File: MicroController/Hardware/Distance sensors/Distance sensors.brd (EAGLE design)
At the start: 70 x 40 mm, 20 parts

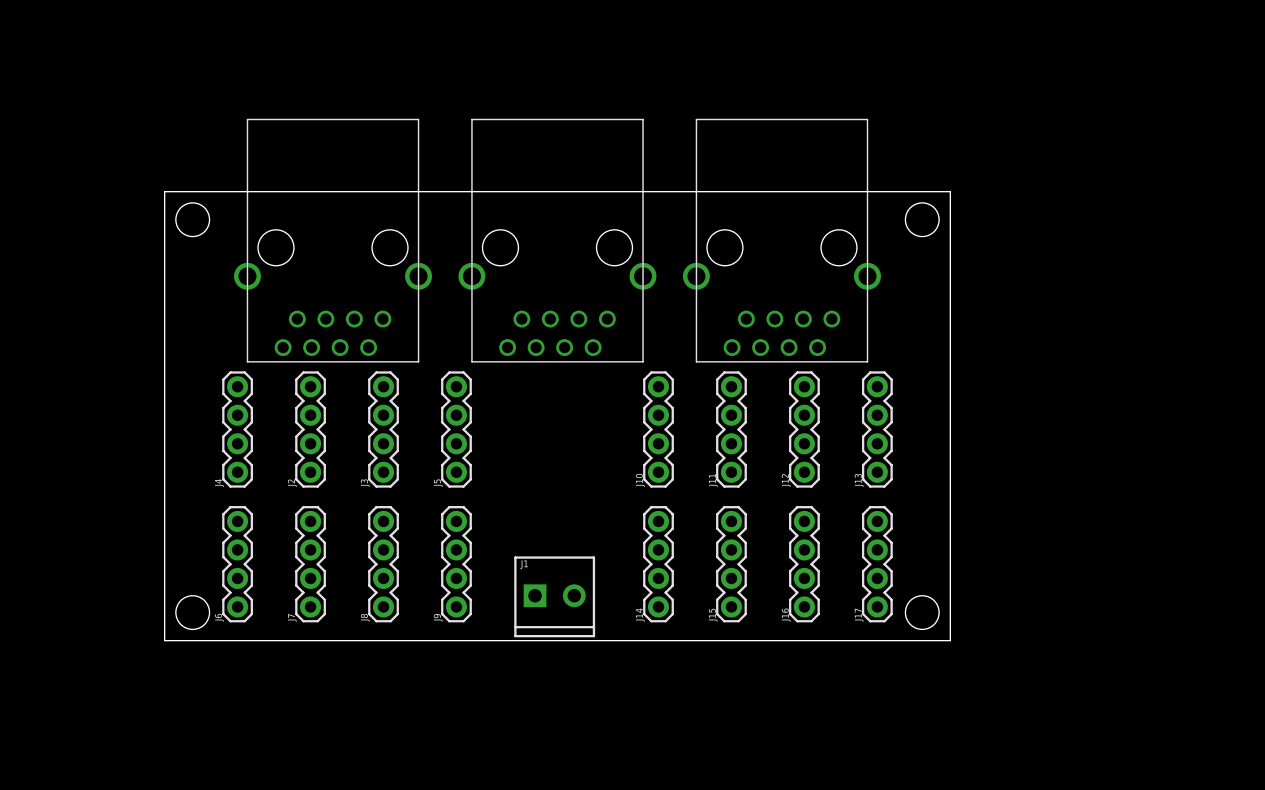
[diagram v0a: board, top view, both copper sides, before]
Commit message: Major improvements
The Ultrasone PCB is in a good place now, it has also been well implemented on the control PCB.
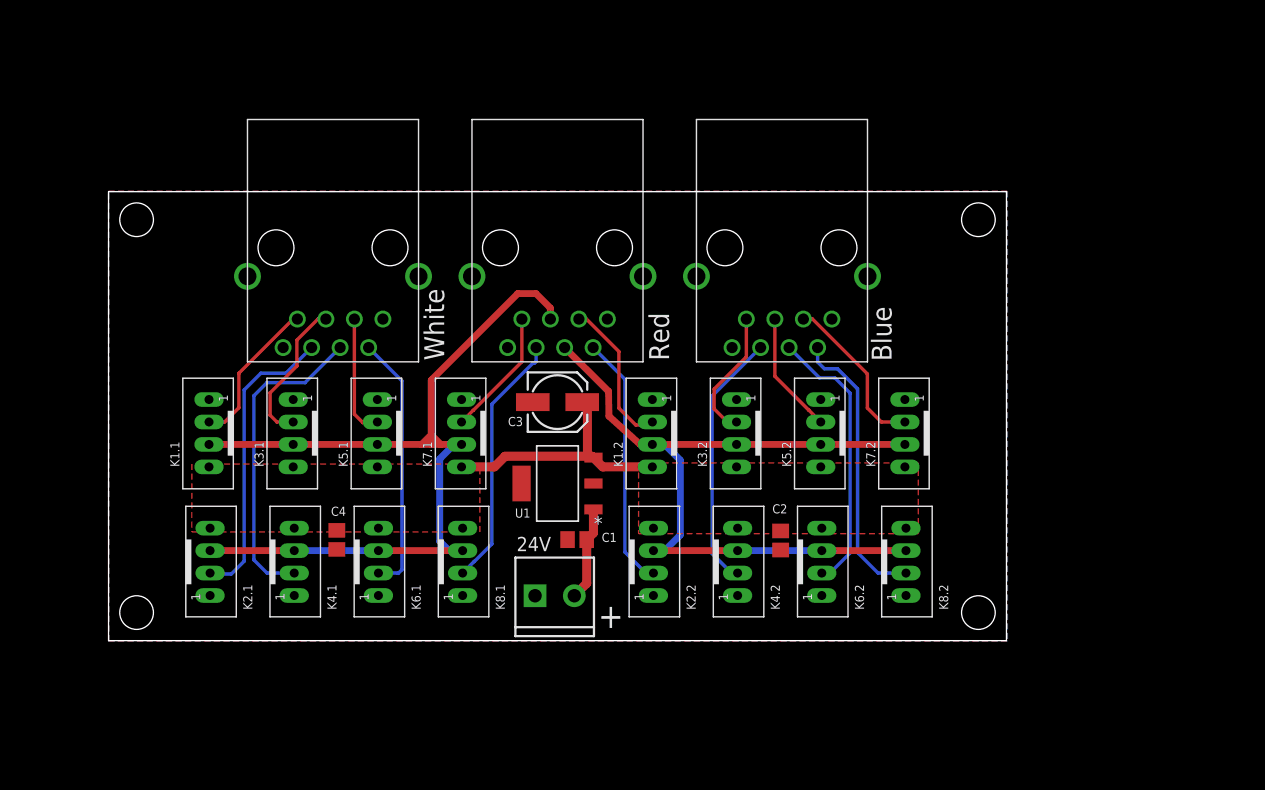
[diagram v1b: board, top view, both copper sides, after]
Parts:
- removed J10, J11, J12, J13, J14, J15, J16, J17, J2, J3, J4, J5, J6, J7, J8, J9: (no value), SparkFun-Connectors:1X04
- added C1, C2, C4: (no value), adafruit:C0805
- added C3: (no value), adafruit:153CLV-0505
- added K1.1, K1.2, K2.1, K2.2, K3.1, K3.2, K4.1, K4.2, K5.1, K5.2, K6.1, K6.2, K7.1, K7.2, K8.1, K8.2: JST-PH_4-PIN_HEADER, SRG:JST_B4B-PH_HEADER
- added U1: LM2937IMP-5.0, NSC_By_element14_Batch_1.1:SOT230P700X180-4N
- renumbered J1 to 24V
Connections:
- new net +5V: C2.1, C3.+, C4.1, K1.1.P4, K1.2.P4, K2.1.P4, K2.2.P4, K3.1.P4, K3.2.P4, K4.1.P4, K4.2.P4, K5.1.P4, K5.2.P4, K6.1.P4, K6.2.P4, K7.1.P4, K7.2.P4, K8.1.P4, K8.2.P4, U1.3
- new net GND: 24V.1, C1.2, C2.2, C3.-, C4.2, K1.1.P1, K1.2.P1, K2.1.P1, K2.2.P1, K3.1.P1, K3.2.P1, K4.1.P1, K4.2.P1, K5.1.P1, K5.2.P1, K6.1.P1, K6.2.P1, K7.1.P1, K7.2.P1, K8.1.P1, K8.2.P1, U$1.1, U$1.8, U$1.GND1, U$1.GND2, U$2.1, U$2.8, U$2.GND1, U$2.GND2, U$3.1, U$3.8, U$3.GND1, U$3.GND2, U1.2, U1.4
- new net N$1: 24V.2, C1.1, U1.1
- new net TRIGGER_1: K1.1.P3, K2.1.P3, K3.1.P3, K4.1.P3, K5.1.P3, K6.1.P3, K7.1.P3, K8.1.P3, U$2.5
- new net TRIGGER_2: K1.2.P3, K2.2.P3, K3.2.P3, K4.2.P3, K5.2.P3, K6.2.P3, K7.2.P3, K8.2.P3, U$2.4
- new net ULTRA1: K1.1.P2, U$1.7
- new net ULTRA10: K2.2.P2, U$2.2
- new net ULTRA11: K3.2.P2, U$3.7
- new net ULTRA12: K4.2.P2, U$3.6
- new net ULTRA13: K5.2.P2, U$3.5
- new net ULTRA14: K6.2.P2, U$3.4
- new net ULTRA15: K7.2.P2, U$3.3
- new net ULTRA16: K8.2.P2, U$3.2
- new net ULTRA2: K2.1.P2, U$1.6
- new net ULTRA3: K3.1.P2, U$1.5
- new net ULTRA4: K4.1.P2, U$1.4
- new net ULTRA5: K5.1.P2, U$1.3
- new net ULTRA6: K6.1.P2, U$1.2
- new net ULTRA7: K7.1.P2, U$2.7
- new net ULTRA8: K8.1.P2, U$2.6
- new net ULTRA9: K1.2.P2, U$2.3
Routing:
- net TRIGGER_1: track 0.00 -> 80.7 mm
- net TRIGGER_2: track 0.00 -> 70.3 mm
- net ULTRA4: track 0.00 -> 28.2 mm
- net ULTRA2: track 0.00 -> 26.4 mm
- net ULTRA16: track 0.00 -> 25.5 mm
- net ULTRA14: track 0.00 -> 24.6 mm
- net ULTRA6: track 0.00 -> 23.3 mm
- net ULTRA12: track 0.00 -> 23.1 mm
- net ULTRA8: track 0.00 -> 22.9 mm
- net +5V: track 0.00 -> 22.8 mm
- net ULTRA10: track 0.00 -> 22.7 mm
- net ULTRA15: track 0.00 -> 14.6 mm
- net ULTRA9: track 0.00 -> 13.5 mm
- net ULTRA1: track 0.00 -> 13.5 mm
- net ULTRA3: track 0.00 -> 13.3 mm
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- added copper zone on layer 1, net +5V
- added copper zone on layer 1, net GND
- added copper zone on layer 16, net GND
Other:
- board size 70 x 40 mm -> 80 x 40 mm
- board text added: "+"
- board text added: "Blue"
- board text added: "Red"
- board text added: "White"

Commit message: Started a redesign of the Distance sensor PCB.
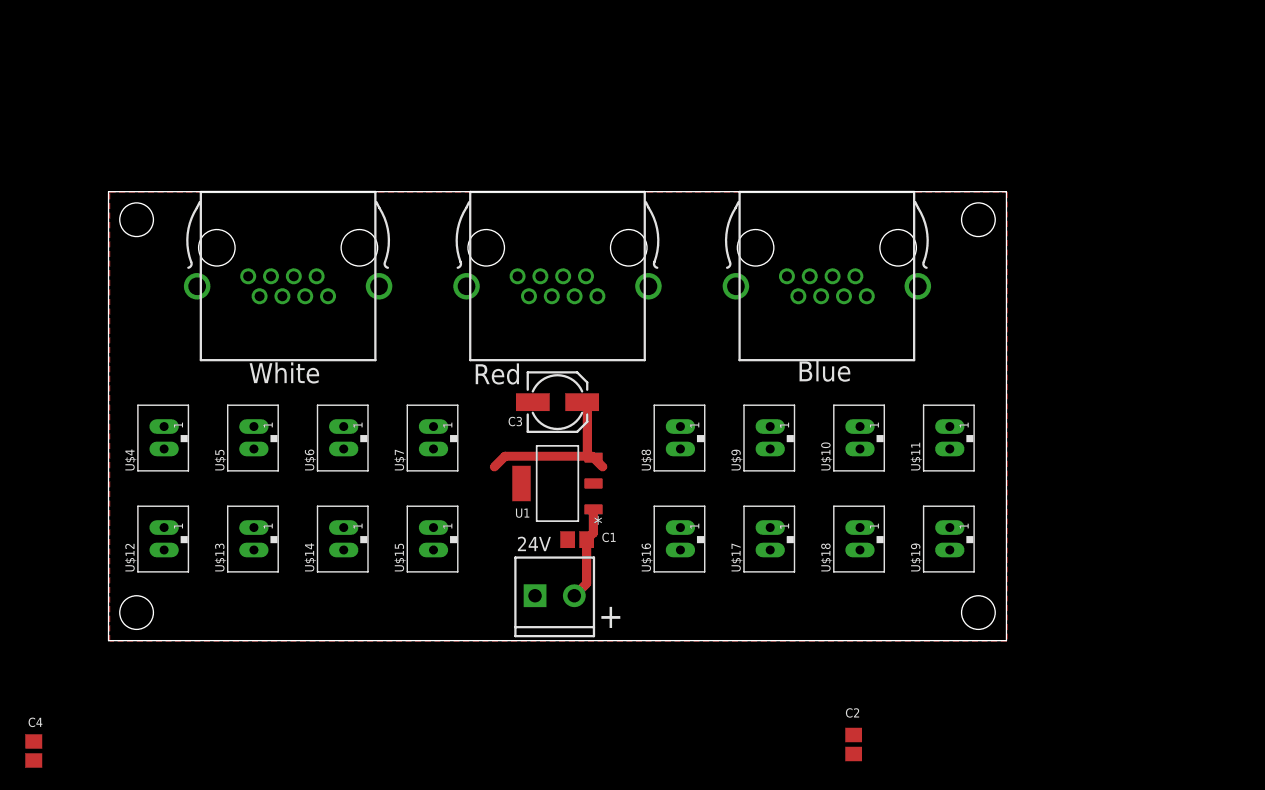
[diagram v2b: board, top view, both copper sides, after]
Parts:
- removed K1.1, K1.2, K2.1, K2.2, K3.1, K3.2, K4.1, K4.2, K5.1, K5.2, K6.1, K6.2, K7.1, K7.2, K8.1, K8.2: JST-PH_4-PIN_HEADER, SRG:JST_B4B-PH_HEADER
- removed U$1, U$2, U$3: RJ45-TRAFO, con-amphenol-rj45-ld:RJ45-TRAFO
- added U$10, U$11, U$12, U$13, U$14, U$15, U$16, U$17, U$18, U$19, U$4, U$5, U$6, U$7, U$8, U$9: JST-PH_2-PIN_HEADER, SRG:JST_B2B-PH_HEADER
- added X1, X2, X3: 0446200002, con-molex:0446200002
- moved C4 32.9 mm to (-11.7, -9.83)
- moved C2 19.3 mm to (61.4, -9.26)
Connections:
- net +5V: no longer K1.1.P4, K1.2.P4, K2.1.P4, K2.2.P4, K3.1.P4, K3.2.P4, K4.1.P4, K4.2.P4, K5.1.P4, K5.2.P4, K6.1.P4, K6.2.P4, K7.1.P4, K7.2.P4, K8.1.P4, K8.2.P4
- net GND: now also X1.1, X1.8, X1.S@1, X1.S@2, X2.1, X2.8, X2.S@1, X2.S@2, X3.1, X3.8, X3.S@1, X3.S@2; no longer K1.1.P1, K1.2.P1, K2.1.P1, K2.2.P1, K3.1.P1, K3.2.P1, K4.1.P1, K4.2.P1, K5.1.P1, K5.2.P1, K6.1.P1, K6.2.P1, K7.1.P1, K7.2.P1, K8.1.P1, K8.2.P1, U$1.1, U$1.8, U$1.GND1, U$1.GND2, U$2.1, U$2.8, U$2.GND1, U$2.GND2, U$3.1, U$3.8, U$3.GND1, U$3.GND2
- net TRIGGER_1: now also U$12.P2, U$13.P2, U$14.P2, U$15.P2, U$4.P2, U$5.P2, U$6.P2, U$7.P2, X2.4; no longer K1.1.P3, K2.1.P3, K3.1.P3, K4.1.P3, K5.1.P3, K6.1.P3, K7.1.P3, K8.1.P3, U$2.5
- net TRIGGER_2: now also U$10.P2, U$11.P2, U$16.P2, U$17.P2, U$18.P2, U$19.P2, U$8.P2, U$9.P2, X2.5; no longer K1.2.P3, K2.2.P3, K3.2.P3, K4.2.P3, K5.2.P3, K6.2.P3, K7.2.P3, K8.2.P3, U$2.4
- net ULTRA1: now also U$4.P1, X1.2; no longer K1.1.P2, U$1.7
- net ULTRA10: now also U$16.P1, X2.6; no longer K2.2.P2, U$2.2
- net ULTRA11: now also U$9.P1, X3.2; no longer K3.2.P2, U$3.7
- net ULTRA12: now also U$17.P1, X3.3; no longer K4.2.P2, U$3.6
- net ULTRA13: now also U$10.P1, X3.4; no longer K5.2.P2, U$3.5
- net ULTRA14: now also U$18.P1, X3.5; no longer K6.2.P2, U$3.4
- net ULTRA15: now also U$11.P1, X3.6; no longer K7.2.P2, U$3.3
- net ULTRA16: now also U$19.P1, X3.7; no longer K8.2.P2, U$3.2
- net ULTRA2: now also U$12.P1, X1.3; no longer K2.1.P2, U$1.6
- net ULTRA3: now also U$5.P1, X1.4; no longer K3.1.P2, U$1.5
- net ULTRA4: now also U$13.P1, X1.5; no longer K4.1.P2, U$1.4
- net ULTRA5: now also U$6.P1, X1.6; no longer K5.1.P2, U$1.3
- net ULTRA6: now also U$14.P1, X1.7; no longer K6.1.P2, U$1.2
- net ULTRA7: now also U$7.P1, X2.2; no longer K7.1.P2, U$2.7
- net ULTRA8: now also U$15.P1, X2.3; no longer K8.1.P2, U$2.6
- net ULTRA9: now also U$8.P1, X2.7; no longer K1.2.P2, U$2.3
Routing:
- net TRIGGER_1: track 80.7 -> 0.00 mm
- net TRIGGER_2: track 70.3 -> 0.00 mm
- net ULTRA4: track 28.2 -> 0.00 mm
- net ULTRA2: track 26.4 -> 0.00 mm
- net ULTRA16: track 25.5 -> 0.00 mm
- net ULTRA14: track 24.6 -> 0.00 mm
- net ULTRA6: track 23.3 -> 0.00 mm
- net ULTRA12: track 23.1 -> 0.00 mm
- net ULTRA8: track 22.9 -> 0.00 mm
- net ULTRA10: track 22.7 -> 0.00 mm
- net ULTRA15: track 14.6 -> 0.00 mm
- net ULTRA9: track 13.5 -> 0.00 mm
- net ULTRA1: track 13.5 -> 0.00 mm
- net ULTRA3: track 13.3 -> 0.00 mm
- net ULTRA11: track 11.7 -> 0.00 mm
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- removed copper zone on layer 1, net +5V
- removed copper zone on layer 16, net GND

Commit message: Many changes to the Ultrasone sensor PCB.
Added a lot op components.
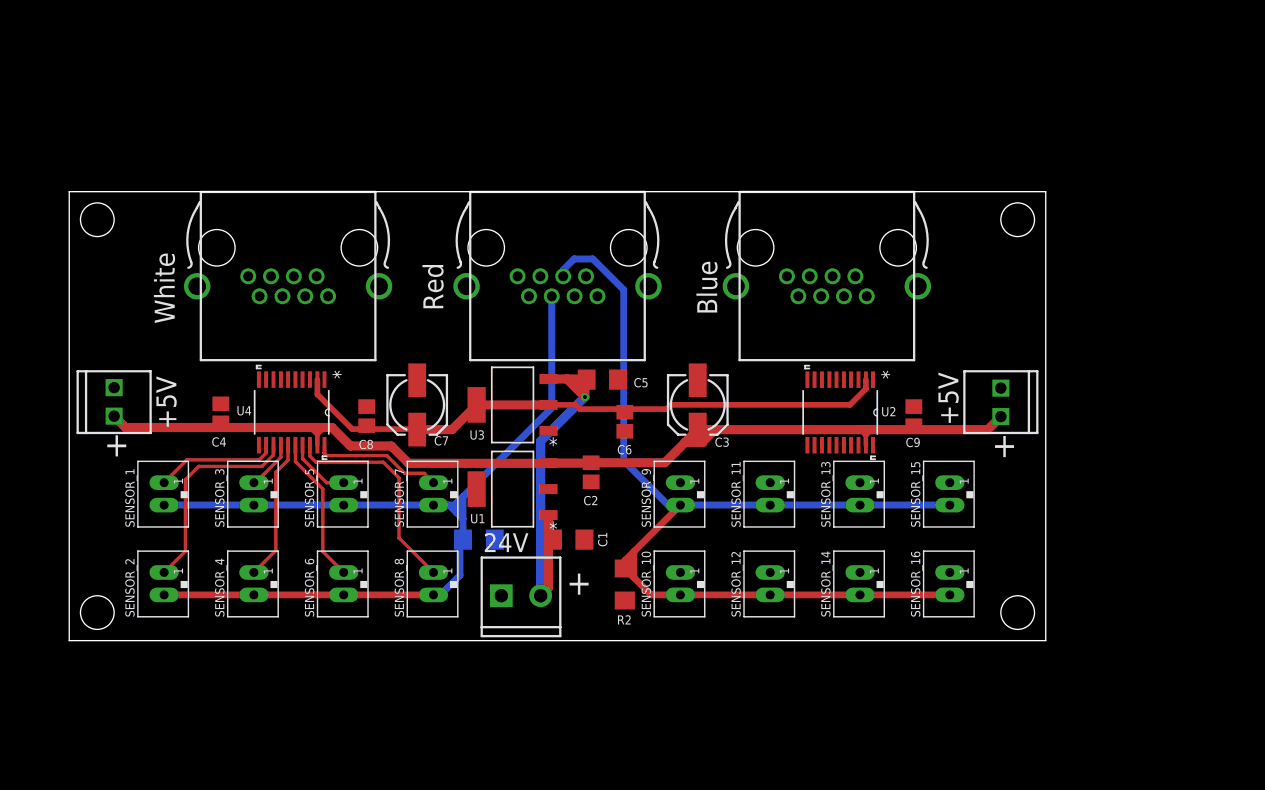
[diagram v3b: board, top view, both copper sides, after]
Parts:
- removed U$10, U$11, U$12, U$13, U$14, U$15, U$16, U$17, U$18, U$19, U$4, U$5, U$6, U$7, U$8, U$9: JST-PH_2-PIN_HEADER, SRG:JST_B2B-PH_HEADER
- added 5V, J1: (no value), SparkFun-Connectors:1X02_2.54_SCREWTERM
- added C5: (no value), adafruit:C1206
- added C6, C8, C9: (no value), adafruit:C0805
- added C7: (no value), adafruit:153CLV-0505
- added R1, R2: (no value), adafruit:R1206
- added SENSOR_1, SENSOR_10, SENSOR_11, SENSOR_12, SENSOR_13, SENSOR_14, SENSOR_15, SENSOR_16, SENSOR_2, SENSOR_3, SENSOR_4, SENSOR_5, SENSOR_6, SENSOR_7, SENSOR_8, SENSOR_9: JST-PH_2-PIN_HEADER, SRG:JST_B2B-PH_HEADER
- added U2, U4: TXB0108PWR, Texas Instruments_By_element14_Batch_1:SOP65P640X120-20N
- added U3: TLV1117-33CDCY, Texas Instruments_By_element14_Batch_1:SOT230P700X180-4N
- C1: device adafruit:C0805 -> adafruit:C1206
- moved C4 34.4 mm to (5.00, 20.2), turned to 90 degrees
- moved C2 33.7 mm to (38.0, 15.0)
- moved C3 12.5 mm to (47.5, 21.0), turned to 270 degrees
- moved U1 4.03 mm to (31.0, 13.5)
- moved 24V 3.00 mm to (30.0, 4.00)
- moved C1 0.75 mm to (36.0, 9.00), turned to 0 degrees
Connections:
- new net +24V: 24V.2, C1.1, C5.1, U1.1, U3.3
- new net +3V3: C6.1, C7.+, C8.1, U2.2, U3.2, U3.4, U4.2
- new net N$2: U4.3
- new net N$3: U4.4
- new net N$4: U4.5
- new net N$5: U4.6
- new net N$6: U4.7
- new net N$7: U4.8
- new net N$8: U4.9
- new net ULTRAS1: SENSOR_1.P1, U4.12
- new net ULTRAS10: SENSOR_10.P1
- new net ULTRAS11: SENSOR_11.P1
- new net ULTRAS12: SENSOR_12.P1
- new net ULTRAS13: SENSOR_13.P1
- new net ULTRAS14: SENSOR_14.P1
- new net ULTRAS15: SENSOR_15.P1
- new net ULTRAS16: SENSOR_16.P1
- new net ULTRAS2: SENSOR_2.P1, U4.13
- new net ULTRAS3: SENSOR_3.P1, U4.14
- new net ULTRAS4: SENSOR_4.P1, U4.15
- new net ULTRAS5: SENSOR_5.P1, U4.17
- new net ULTRAS6: SENSOR_6.P1, U4.16
- new net ULTRAS7: SENSOR_7.P1, U4.20
- new net ULTRAS8: SENSOR_8.P1, U4.18
- new net ULTRAS9: SENSOR_9.P1
- net +5V: now also 5V.P2, C9.1, J1.P1, U2.19, U4.19
- net GND: now also 5V.P1, C5.2, C6.2, C7.-, C8.2, C9.2, J1.P2, R1.1, R2.1, U2.11, U3.1, U4.11
- net N$1: now also U4.1; no longer 24V.2, C1.1, U1.1
- net TRIGGER_1: now also R1.2, SENSOR_1.P2, SENSOR_2.P2, SENSOR_3.P2, SENSOR_4.P2, SENSOR_5.P2, SENSOR_6.P2, SENSOR_7.P2, SENSOR_8.P2; no longer U$12.P2, U$13.P2, U$14.P2, U$15.P2, U$4.P2, U$5.P2, U$6.P2, U$7.P2
- net TRIGGER_2: now also R2.2, SENSOR_10.P2, SENSOR_11.P2, SENSOR_12.P2, SENSOR_13.P2, SENSOR_14.P2, SENSOR_15.P2, SENSOR_16.P2, SENSOR_9.P2; no longer U$10.P2, U$11.P2, U$16.P2, U$17.P2, U$18.P2, U$19.P2, U$8.P2, U$9.P2
- net ULTRA1: no longer U$4.P1
- net ULTRA10: no longer U$16.P1
- net ULTRA11: no longer U$9.P1
- net ULTRA12: no longer U$17.P1
- net ULTRA13: no longer U$10.P1
- net ULTRA14: no longer U$18.P1
- net ULTRA15: no longer U$11.P1
- net ULTRA16: no longer U$19.P1
- net ULTRA2: no longer U$12.P1
- net ULTRA3: no longer U$5.P1
- net ULTRA4: no longer U$13.P1
- net ULTRA5: no longer U$6.P1
- net ULTRA6: no longer U$14.P1
- net ULTRA7: no longer U$7.P1
- net ULTRA8: no longer U$15.P1
- net ULTRA9: no longer U$8.P1
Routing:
- net TRIGGER_2: track 0.00 -> 93.4 mm
- net TRIGGER_1: track 0.00 -> 86.4 mm
- net +5V: track 15.5 -> 93.1 mm
- net +3V3: track 0.00 -> 54.9 mm
- net +24V: track 0.00 -> 34.7 mm, vias 0 -> 1
- net ULTRAS8: track 0.00 -> 19.4 mm
- net ULTRAS2: track 0.00 -> 18.7 mm
- net ULTRAS6: track 0.00 -> 13.1 mm
- net ULTRAS4: track 0.00 -> 12.6 mm
- net ULTRAS7: track 0.00 -> 11.6 mm
- net ULTRAS1: track 0.00 -> 10.9 mm
- net N$1: track 8.39 -> 0.00 mm
- net ULTRAS5: track 0.00 -> 5.76 mm
- net ULTRAS3: track 0.00 -> 4.42 mm
- removed copper zone on layer 1, net GND
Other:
- board size 80 x 40 mm -> 87 x 40 mm
- board text added: "+5V"
